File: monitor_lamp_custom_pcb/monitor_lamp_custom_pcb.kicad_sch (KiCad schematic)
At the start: 25 parts, among them IC1 HUSB238, J1 USB_C_Receptacle_PowerOnly_6P, J6 Direct_power_supply, Q1 AO3401A, U1 TPS563300, U2 TPS561208DDCT

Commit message: Added some LCSC to the components
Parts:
- IC1: LCSC (none) -> C7471904
- J1: LCSC (none) -> C2894893
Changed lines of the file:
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@@
+			)
+		)
+		(property "LCSC" "C2894893"
+			(at 33.02 45.72 0)
+			(hide yes)
+			(show_name no)
+			(do_not_autoplace no)
+			(effects
+				(font
+					(size 1.27 1.27)
+				)
 			)
 		)
@@
 			)
 		)
+		(property "LCSC" "C7471904"
+			(at 107.95 43.18 0)
+			(hide yes)
+			(show_name no)
+			(do_not_autoplace no)
+			(effects
+				(font
+					(size 1.27 1.27)
+				)
+			)
+		)

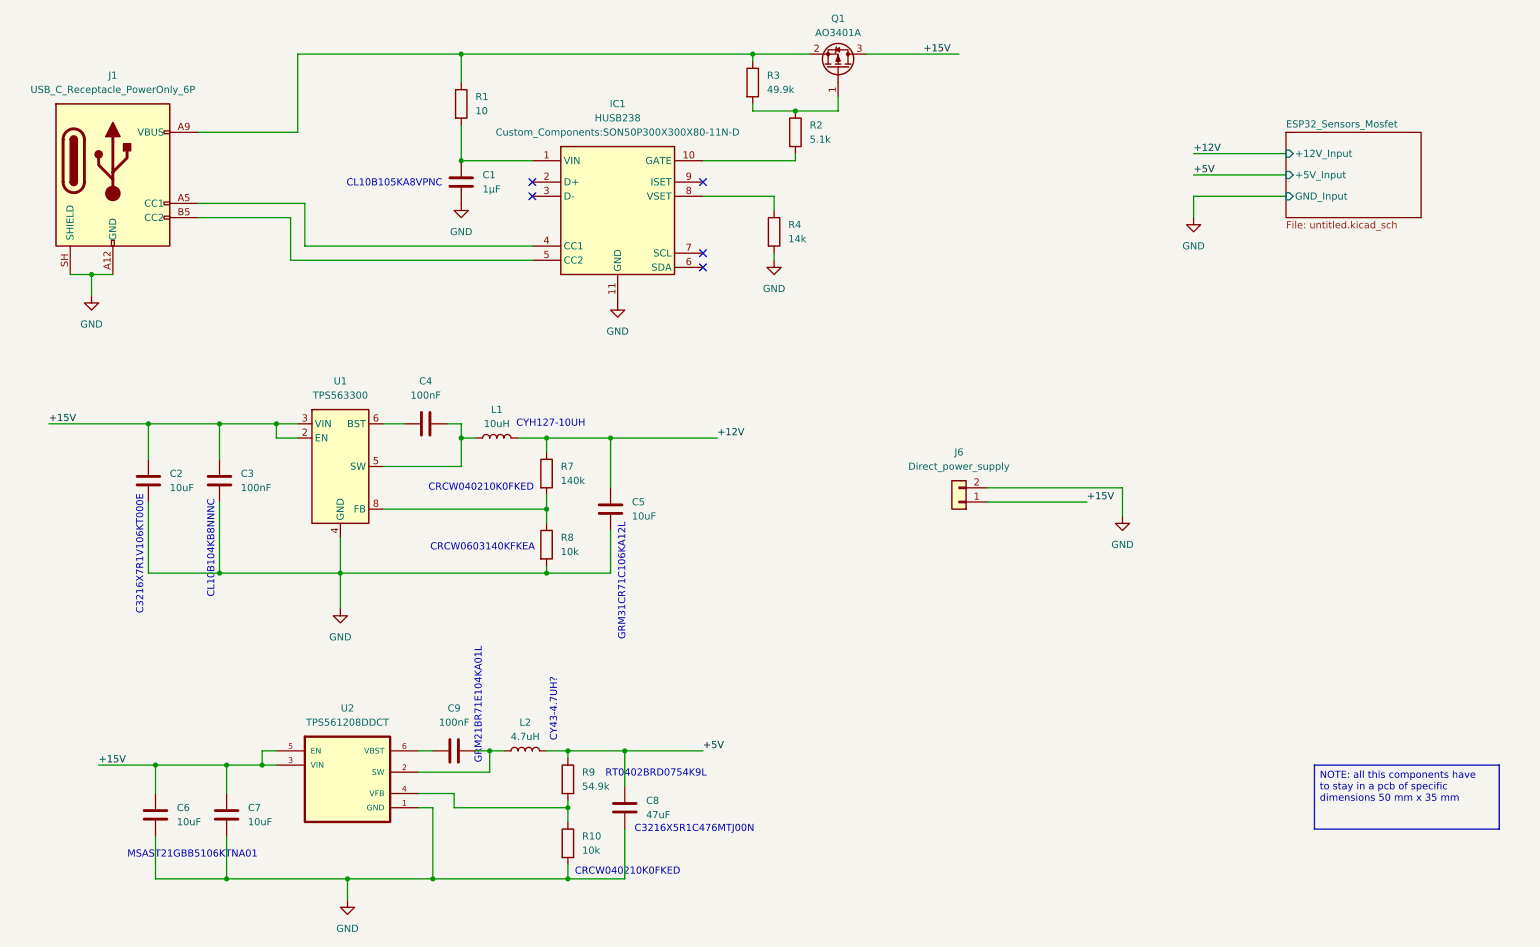
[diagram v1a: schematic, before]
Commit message: Assign LCSC number to some component and selected new voltage regulator
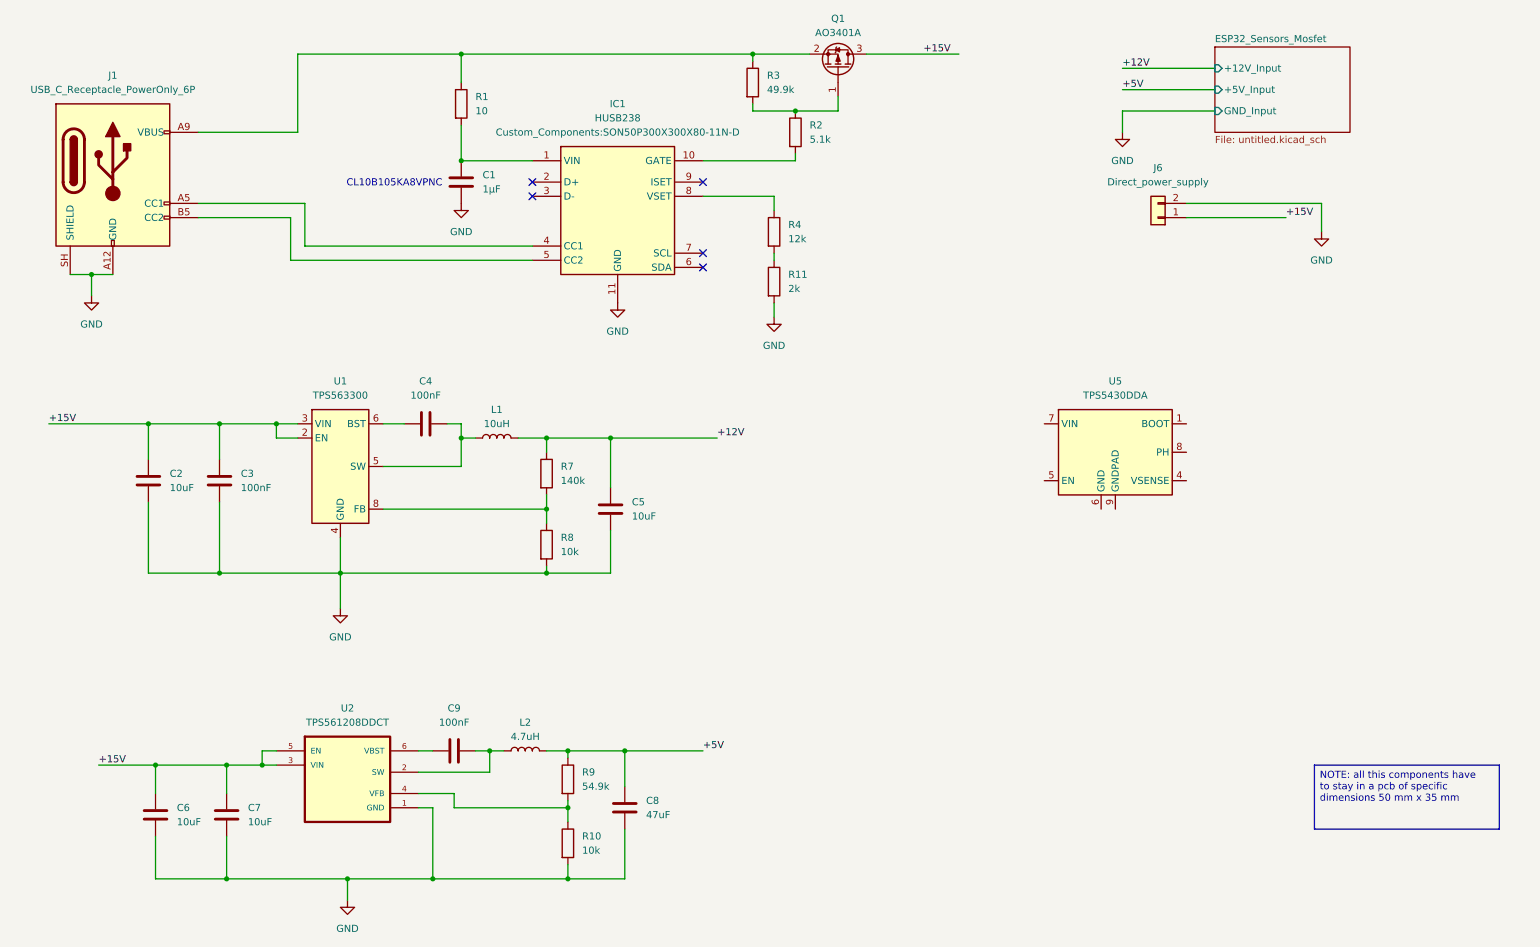
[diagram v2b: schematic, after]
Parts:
- added R11: 2k, Resistor_SMD:R_0402_1005Metric, symbol Device:R
- added U5: TPS5430DDA, Package_SO:TI_SO-PowerPAD-8_ThermalVias, symbol Regulator_Switching:TPS5430DDA
- Q1: LCSC (none) -> C15127
- R1: LCSC (none) -> C22859
- R2: LCSC (none) -> C23186
- R3: LCSC (none) -> C23184
- R4: value 14k -> 12k; footprint Resistor_SMD:R_0603_1608Metric -> Resistor_SMD:R_0402_1005Metric; LCSC (none) -> C25752
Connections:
- net GND: now also R11.2; no longer R4.2
- new net: R11.1, R4.2
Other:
- note removed: "C3216X5R1C476MTJ00N"
- note removed: "C3216X7R1V106KT000E"
- note removed: "CL10B104KB8NNNC"
- note removed: "CRCW040210K0FKED"
- note removed: "CRCW0603140KFKEA"
- note removed: "CY43-4.7UH?"
- note removed: "CYH127-10UH"
- note removed: "GRM21BR71E104KA01L"
- note removed: "GRM31CR71C106KA12L"
- note removed: "MSAST21GBB5106KTNA01"
- note removed: "RT0402BRD0754K9L"
- moved on the sheet: J6

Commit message: Drastic change
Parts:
- removed L1: 10uH, Inductor_SMD:L_SXN_SMDRI124, symbol Device:L
- removed L2: 4.7uH, Inductor_SMD:L_Murata_LQH55DN_5.7x5.0mm, symbol Device:L
- removed R10, R8: 10k, Resistor_SMD:R_0603_1608Metric, symbol Device:R
- removed R7: 140k, Resistor_SMD:R_0603_1608Metric, symbol Device:R
- removed R9: 54.9k, Resistor_SMD:R_0603_1608Metric, symbol Device:R
- removed U1: TPS563300, Package_TO_SOT_SMD:SOT-583-8, symbol Regulator_Switching:TPS563300
- removed U2: TPS561208DDCT, Custom_Components:SOT95P280X110-6N, symbol TPS56120:TPS561208DDCT
- added D2, D3: SS14, Diode_SMD:D_SMA, symbol Diode:SS14
- added L3: 22uH, symbol Device:L
- added L4: 68uH, symbol Device:L
- added R12, R14: 10k, Resistor_SMD:R_0603_1608Metric, symbol Device:R
- added R13: 1.1k, Resistor_SMD:R_0603_1608Metric, symbol Device:R
- added R15: 3.3k, Resistor_SMD:R_0603_1608Metric, symbol Device:R
- added U6: TPS5430DDA, Package_SO:TI_SO-PowerPAD-8_ThermalVias, symbol Regulator_Switching:TPS5430DDA
- C1: footprint Capacitor_SMD:C_0603_1608Metric -> Capacitor_SMD:C_0402_1005Metric; LCSC (none) -> C52923
- C2: value 10uF -> 22uF; footprint Capacitor_SMD:C_0805_2012Metric -> Capacitor_SMD:C_0603_1608Metric; LCSC (none) -> C59461
- C3: value 100nF -> 22uF; LCSC (none) -> C59461
- C4: value 100nF -> 10nF; LCSC (none) -> C15195
- C5: value 10uF -> 100uF; footprint Capacitor_SMD:C_1206_3216Metric -> (none)
- C6, C7: footprint Capacitor_SMD:C_0805_2012Metric -> Capacitor_SMD:C_0603_1608Metric; LCSC (none) -> C96446
- C8: value 47uF -> 10nF; footprint Capacitor_SMD:C_1206_3216Metric -> Capacitor_SMD:C_0402_1005Metric; LCSC (none) -> C15195
- C9: value 100nF -> 100uF; footprint Capacitor_SMD:C_0805_2012Metric -> (none)
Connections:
- net +12V: now also L3.2, R12.1
- net +15V: now also U5.7 (VIN), U6.7 (VIN)
- net +5V: now also C9.1, L4.2, R14.1; no longer C8.1
- net GND: now also U5.9 (GNDPAD), D2.2 (A), D3.2 (A), U6.9 (GNDPAD); no longer C2.2, C3.2, C5.2, C6.2, C7.2, C8.2
- net at C4.2: now also U5.8 (PH), D2.1 (K), L3.1
- net at C9.2: now also C6.2, C7.2, R15.2, U6.6 (GND)
- net at C4.1: now also U5.1 (BOOT)
- net at U5.4 (VSENSE): now also R12.2, R13.1
- net at U5.6 (GND): now also C2.2, C3.2, C5.2, R13.2
- new net: C8.2, D3.1 (K), L4.1, U6.8 (PH)
- new net: R14.2, R15.1, U6.4 (VSENSE)
- new net: C8.1, U6.1 (BOOT)
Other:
- note removed: "CL10B105KA8VPNC"
- moved on the sheet: J6, U5

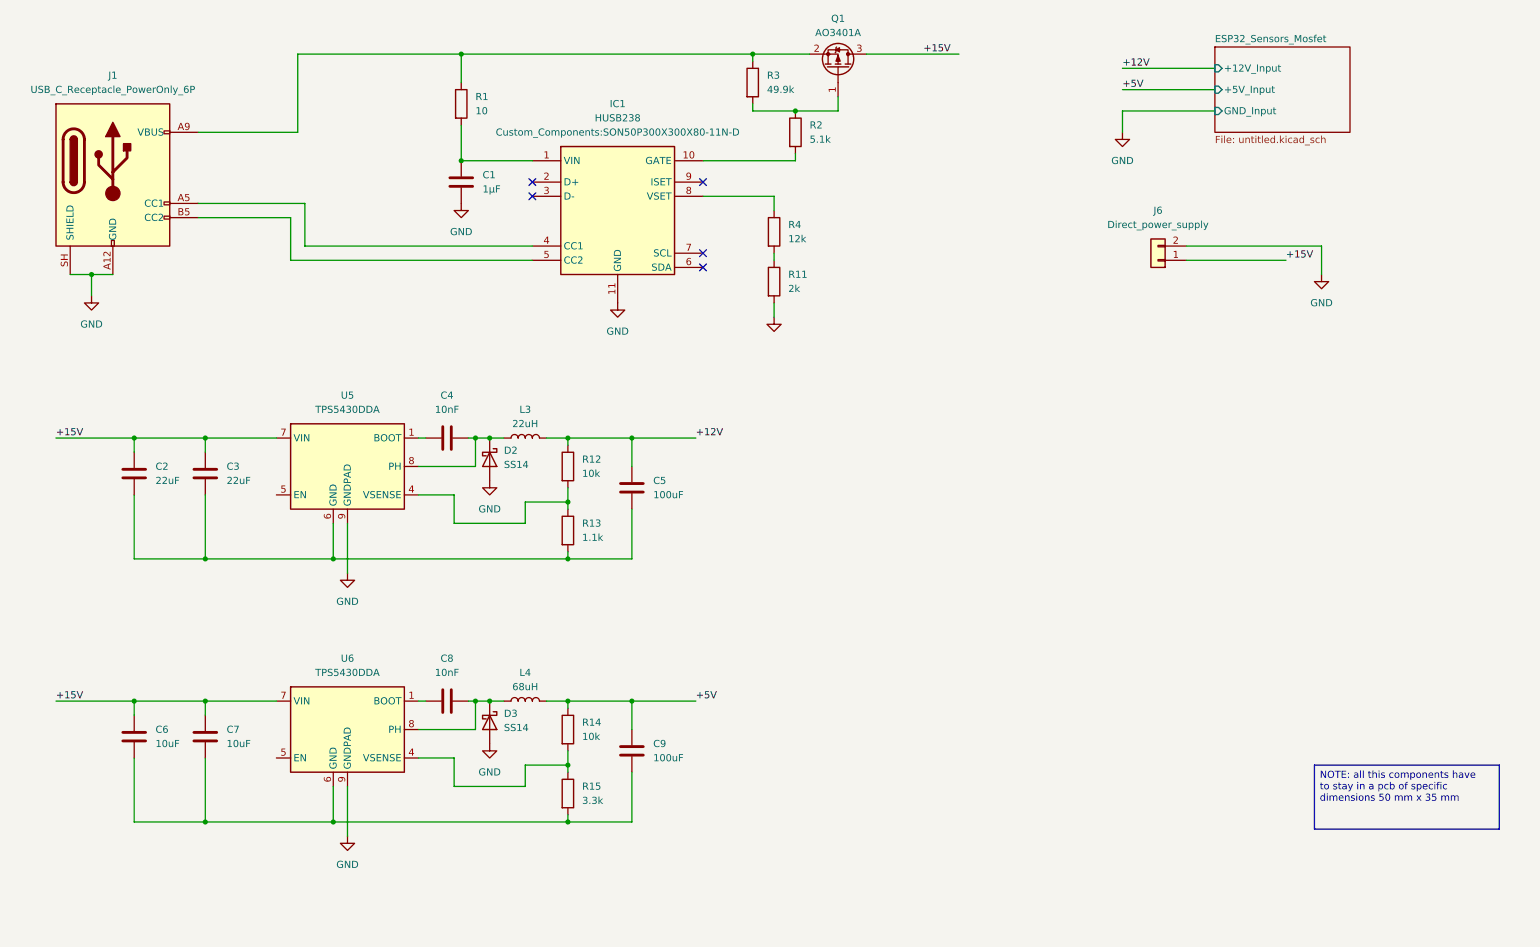
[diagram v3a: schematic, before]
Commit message: Remodelled the scheme with 12V input
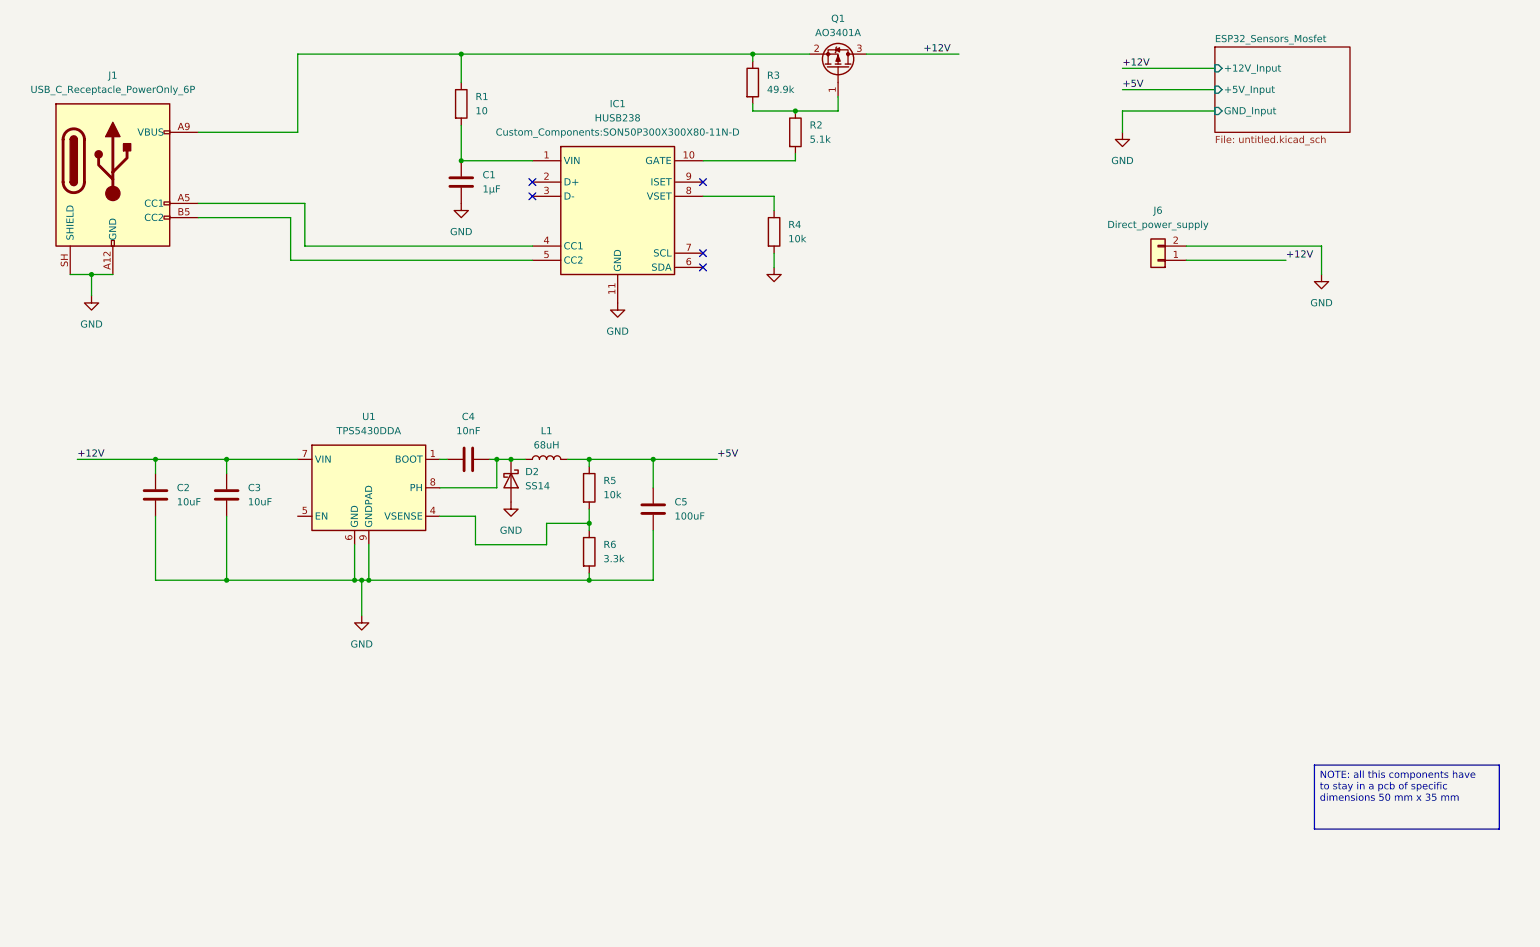
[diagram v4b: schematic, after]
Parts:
- removed C2, C3: 22uF, Capacitor_SMD:C_0603_1608Metric, symbol Device:C
- removed C4: 10nF, Capacitor_SMD:C_0402_1005Metric, symbol Device:C
- removed C5: 100uF, symbol Device:C
- removed D2: SS14, Diode_SMD:D_SMA, symbol Diode:SS14
- removed L3: 22uH, symbol Device:L
- removed R11: 2k, Resistor_SMD:R_0402_1005Metric, symbol Device:R
- removed R12: 10k, Resistor_SMD:R_0603_1608Metric, symbol Device:R
- removed R13: 1.1k, Resistor_SMD:R_0603_1608Metric, symbol Device:R
- removed U5: TPS5430DDA, Package_SO:TI_SO-PowerPAD-8_ThermalVias, symbol Regulator_Switching:TPS5430DDA
- C5: renamed from C9; footprint (none) -> Capacitor_SMD:CP_Elec_6.3x5.4
- L1: renamed from L4; footprint (none) -> components:L_Sumida_CD75
- R4: value 12k -> 10k; LCSC C25752 -> C25744
- renumbered C6 to C2, C7 to C3, C8 to C4, D3 to D2, R14 to R5, R15 to R6, U6 to U1
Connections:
- net +15V is gone; now on net +12V: C2.1, C3.1, J6.1 (Pin_1), Q1.3 (D), U1.7 (VIN)
- net GND: now also C2.2, C3.2, C5.2, R4.2, R6.2, U1.6 (GND)
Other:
- moved on the sheet: C2, C3, C4, C5, D2, L1, R5, R6, U1

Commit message: Placed connection pad
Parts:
- added J5, J7: Conn_01x01, Connector_Wire:SolderWirePad_1x01_SMD_2x4mm, symbol Connector_Generic:Conn_01x01
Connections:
- net +12V: now also J5.1 (Pin_1)
- net GND: now also J7.1 (Pin_1)

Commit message: Terminated design, generated fabrication files for JLCPCB
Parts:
- C5, J6, L1: now left out of the parts list
- IC1: footprint Custom_Components:SON50P300X300X80-11N-D -> Custom_Components:DFN-10L
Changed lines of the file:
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@@
 		(body_style 1)
 		(exclude_from_sim no)
-		(in_bom yes)
+		(in_bom no)
 		(on_board yes)
 		(in_pos_files yes)
@@
 		(body_style 1)
 		(exclude_from_sim no)
-		(in_bom yes)
+		(in_bom no)
 		(on_board yes)
 		(in_pos_files yes)
@@
 			)
 		)
-		(property "Footprint" "Custom_Components:SON50P300X300X80-11N-D"
+		(property "Footprint" "Custom_Components:DFN-10L"
 			(at 123.19 38.1 0)
 			(show_name no)
@@
 		(body_style 1)
 		(exclude_from_sim no)
-		(in_bom yes)
-		(on_board yes)
-		(in_pos_files yes)
+		(in_bom no)
+		(on_board yes)
+		(in_pos_files yes)

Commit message: Added some drawing to the board and recreated fabbrication file
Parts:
- J1: LCSC C2894893 -> C283540
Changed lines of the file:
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@@
 			)
 		)
-		(property "LCSC" "C2894893"
+		(property "LCSC" "C283540"
 			(at 33.02 45.72 0)
 			(hide yes)

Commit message: Changed connector to JST PH 2.0mm
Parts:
- J1: now left out of the parts list
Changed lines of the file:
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@@
 		(body_style 1)
 		(exclude_from_sim no)
-		(in_bom yes)
+		(in_bom no)
 		(on_board yes)
 		(in_pos_files yes)
